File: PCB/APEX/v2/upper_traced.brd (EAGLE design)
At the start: 160 x 100 mm, 9 parts

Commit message: dimension boards
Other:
- board size 160 x 100 mm -> 72.4 x 23.8 mm
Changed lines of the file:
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@@
 <board>
 <plain>
-<wire x1="0" y1="0" x2="160" y2="0" width="0" layer="20"/>
-<wire x1="160" y1="0" x2="160" y2="100" width="0" layer="20"/>
-<wire x1="160" y1="100" x2="0" y2="100" width="0" layer="20"/>
-<wire x1="0" y1="100" x2="0" y2="0" width="0" layer="20"/>
-<dimension x1="7.62" y1="38.1" x2="80.01" y2="38.1" x3="43.815" y3="29.21" textsize="1.778" layer="1"/>
+<wire x1="7.62" y1="36.83" x2="79.99" y2="36.83" width="0" layer="20"/>
+<wire x1="79.99" y1="36.83" x2="79.99" y2="60.63" width="0" layer="20"/>
+<wire x1="79.99" y1="60.63" x2="7.62" y2="60.63" width="0" layer="20"/>
+<wire x1="7.62" y1="60.63" x2="7.62" y2="36.83" width="0" layer="20"/>
+<dimension x1="7.62" y1="36.83" x2="79.99" y2="36.83" x3="43.805" y3="33.02" textsize="1.778" layer="1"/>
+<dimension x1="79.99" y1="36.83" x2="79.99" y2="60.63" x3="83.82" y3="48.73" textsize="1.778" layer="1"/>
 </plain>
 <attributes>

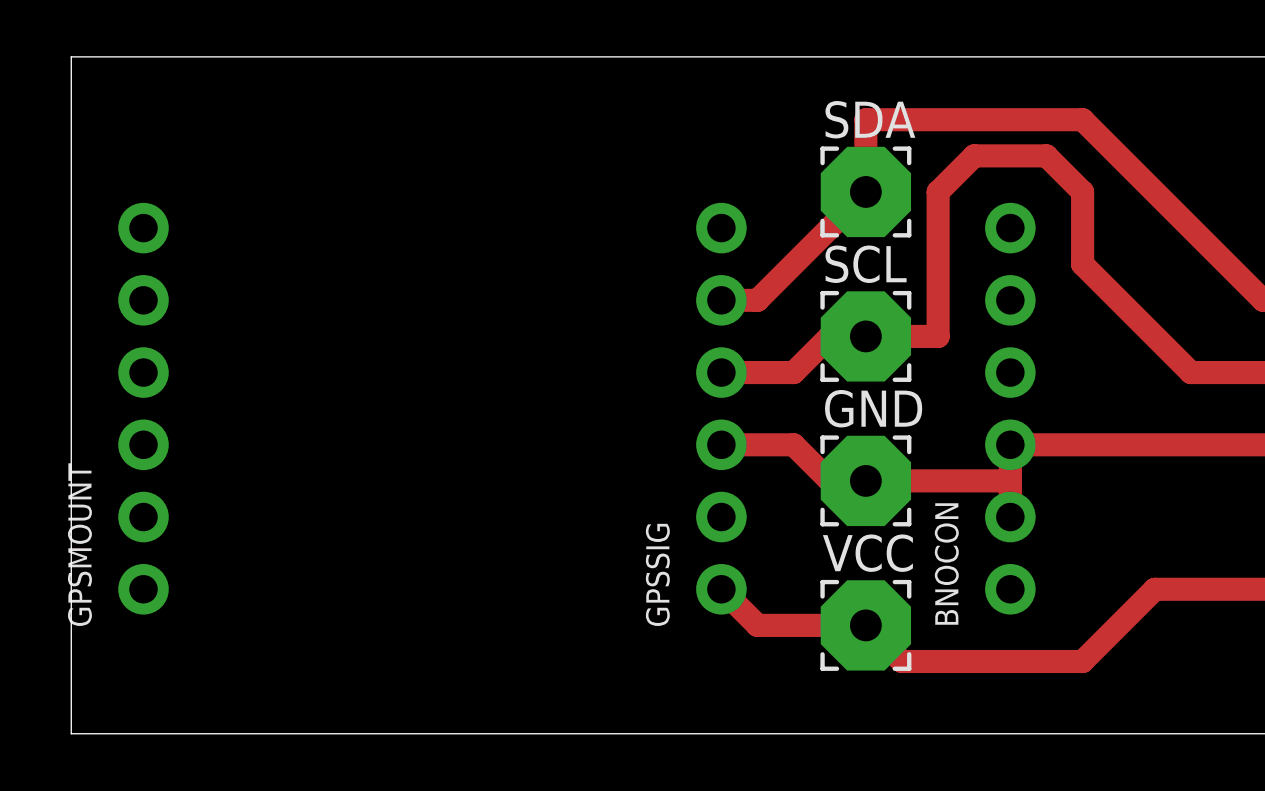
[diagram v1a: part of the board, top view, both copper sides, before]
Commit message: realign sim
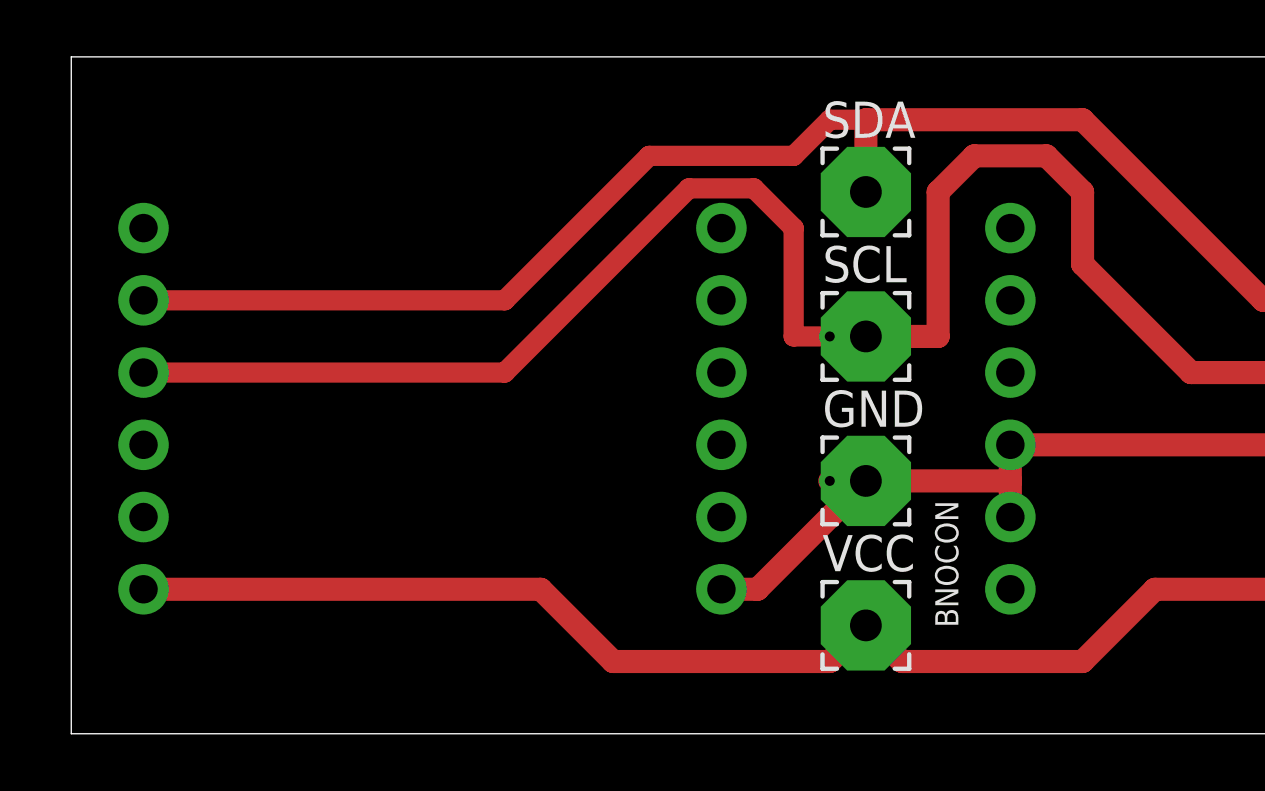
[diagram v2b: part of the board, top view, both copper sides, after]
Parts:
- moved GPSMOUNT 20.3 mm to (30.5, 48.3), flipped to the bottom
- moved GPSSIG 20.3 mm to (10.2, 48.3), flipped to the bottom
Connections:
- net GND: now also GPSMOUNT.1
- net VCC: now also GPSMOUNT.3
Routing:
- net SCL: track 58.3 -> 86.4 mm, vias 0 -> 1
- net VCC: track 49.6 -> 71.0 mm
- net SDA: track 54.3 -> 75.6 mm
- net GND: track 50.6 -> 52.9 mm, vias 0 -> 1
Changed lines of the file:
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@@
 <layer number="16" name="Bottom" color="1" fill="1" visible="yes" active="yes"/>
 <layer number="17" name="Pads" color="2" fill="1" visible="yes" active="yes"/>
-<layer number="18" name="Vias" color="2" fill="1" visible="yes" active="yes"/>
-<layer number="19" name="Unrouted" color="6" fill="1" visible="yes" active="yes"/>
-<layer number="20" name="Dimension" color="24" fill="1" visible="yes" active="yes"/>
-<layer number="21" name="tPlace" color="7" fill="1" visible="yes" active="yes"/>
+<layer number="18" name="Vias" color="2" fill="1" visible="no" active="yes"/>
+<layer number="19" name="Unrouted" color="6" fill="1" visible="no" active="yes"/>
+<layer number="20" name="Dimension" color="24" fill="1" visible="no" active="yes"/>
+<layer number="21" name="tPlace" color="7" fill="1" visible="no" active="yes"/>
 <layer number="22" name="bPlace" color="7" fill="1" visible="yes" active="yes"/>
-<layer number="23" name="tOrigins" color="15" fill="1" visible="yes" active="yes"/>
-<layer number="24" name="bOrigins" color="15" fill="1" visible="yes" active="yes"/>
-<layer number="25" name="tNames" color="7" fill="1" visible="yes" active="yes"/>
-<layer number="26" name="bNames" color="7" fill="1" visible="yes" active="yes"/>
-<layer number="27" name="tValues" color="7" fill="1" visible="yes" active="yes"/>
-<layer number="28" name="bValues" color="7" fill="1" visible="yes" active="yes"/>
+<layer number="23" name="tOrigins" color="15" fill="1" visible="no" active="yes"/>
+<layer number="24" name="bOrigins" color="15" fill="1" visible="no" active="yes"/>
+<layer number="25" name="tNames" color="7" fill="1" visible="no" active="yes"/>
+<layer number="26" name="bNames" color="7" fill="1" visible="no" active="yes"/>
+<layer number="27" name="tValues" color="7" fill="1" visible="no" active="yes"/>
+<layer number="28" name="bValues" color="7" fill="1" visible="no" active="yes"/>
 <layer number="29" name="tStop" color="7" fill="3" visible="no" active="yes"/>
 <layer number="30" name="bStop" color="7" fill="6" visible="no" active="yes"/>
@@
 <layer number="49" name="Reference" color="7" fill="1" visible="yes" active="yes"/>
 <layer number="50" name="dxf" color="7" fill="1" visible="no" active="no"/>
-<layer number="51" name="tDocu" color="7" fill="1" visible="yes" active="yes"/>
-<layer number="52" name="bDocu" color="7" fill="1" visible="yes" active="yes"/>
+<layer number="51" name="tDocu" color="7" fill="1" visible="no" active="yes"/>
+<layer number="52" name="bDocu" color="7" fill="1" visible="no" active="yes"/>
 <layer number="53" name="tGND_GNDA" color="7" fill="9" visible="no" active="no"/>
 <layer number="54" name="bGND_GNDA" color="1" fill="9" visible="no" active="no"/>
@@
 </layers>
 <board>
+<fusionsync huburn="a.YnVzaW5lc3M6bXlpYzM4OA" projecturn="a.YnVzaW5lc3M6bXlpYzM4OCMyMDIwMTEyMTM1NTQyNTgyNg" f3durn="urn:adsk.wipprod:dm.lineage:Sro-rczPQ5WDD7mKh9TVNQ" pcbguid="" lastpulledtime="" lastsyncedchangeguid="" latestrevisionid="8a8f237b-fe8f-4934-b37e-711cd0af9fbb" lastsyncedrevisionid="8a8f237b-fe8f-4934-b37e-711cd0af9fbb" lastboardhashguid="14b4f4f1-fdd0-a5f1-0295-8ed9d9b95309" lastpushedtime="2021-07-01T21:12:17Z" linktopcb3d="true"/>
 <plain>
 <wire x1="7.62" y1="36.83" x2="79.99" y2="36.83" width="0" layer="20"/>
@@
 <wire x1="79.99" y1="60.63" x2="7.62" y2="60.63" width="0" layer="20"/>
 <wire x1="7.62" y1="60.63" x2="7.62" y2="36.83" width="0" layer="20"/>
-<dimension x1="7.62" y1="36.83" x2="79.99" y2="36.83" x3="43.805" y3="33.02" textsize="1.778" layer="1"/>
-<dimension x1="79.99" y1="36.83" x2="79.99" y2="60.63" x3="83.82" y3="48.73" textsize="1.778" layer="1"/>
 </plain>
 <attributes>
@@
 <attribute name="VALUE" x="80.645" y="39.37" size="0.4064" layer="27" ratio="10" rot="R90"/>
 </element>
-<element name="GPSSIG" library="microbuilder" package="1X06_ROUND_70" value="" x="30.48" y="48.26" smashed="yes" rot="R90">
-<attribute name="NAME" x="28.6512" y="40.5638" size="0.8128" layer="25" ratio="18" rot="R90"/>
-<attribute name="VALUE" x="32.385" y="40.64" size="0.4064" layer="27" ratio="10" rot="R90"/>
-</element>
-<element name="GPSMOUNT" library="microbuilder" package="1X06_ROUND_70" value="" x="10.16" y="48.26" smashed="yes" rot="R90">
-<attribute name="NAME" x="8.3312" y="40.5638" size="0.8128" layer="25" ratio="18" rot="R90"/>
-<attribute name="VALUE" x="13.335" y="40.64" size="0.4064" layer="27" ratio="10" rot="R90"/>
+<element name="GPSSIG" library="microbuilder" package="1X06_ROUND_70" value="" x="10.16" y="48.26" smashed="yes" rot="MR90">
+<attribute name="NAME" x="11.9888" y="40.5638" size="0.8128" layer="26" ratio="18" rot="MR90"/>
+<attribute name="VALUE" x="8.255" y="40.64" size="0.4064" layer="28" ratio="10" rot="MR90"/>
+</element>
+<element name="GPSMOUNT" library="microbuilder" package="1X06_ROUND_70" value="" x="30.48" y="48.26" smashed="yes" rot="MR90">
+<attribute name="NAME" x="32.3088" y="40.5638" size="0.8128" layer="26" ratio="18" rot="MR90"/>
+<attribute name="VALUE" x="27.305" y="40.64" size="0.4064" layer="28" ratio="10" rot="MR90"/>
 </element>
 <element name="SCL" library="wirepad" library_urn="urn:adsk.eagle:library:412" package="3,17/1,1" package3d_urn="urn:adsk.eagle:package:30832/1" value="" x="35.56" y="50.8" smashed="yes">
@@
 <wire x1="58.42" y1="46.99" x2="69.85" y2="46.99" width="0.8128" layer="1"/>
 <wire x1="35.56" y1="45.72" x2="34.29" y2="45.72" width="0.8128" layer="1"/>
-<wire x1="34.29" y1="45.72" x2="33.02" y2="46.99" width="0.8128" layer="1"/>
-<wire x1="33.02" y1="46.99" x2="30.48" y2="46.99" width="0.8128" layer="1"/>
 <wire x1="35.56" y1="45.72" x2="40.64" y2="45.72" width="0.8128" layer="1"/>
+<via x="34.29" y="45.72" extent="1-16" drill="0.35"/>
+<contactref element="GPSMOUNT" pad="1"/>
+<wire x1="35.56" y1="45.72" x2="31.75" y2="41.91" width="0.8128" layer="1"/>
+<wire x1="31.75" y1="41.91" x2="30.48" y2="41.91" width="0.8128" layer="1"/>
+<wire x1="10.16" y1="46.99" x2="30.48" y2="41.91" width="0" layer="19" extent="1-1"/>
 </signal>
 <signal name="VCC" class="2">
@@
 <wire x1="36.83" y1="39.37" x2="43.18" y2="39.37" width="0.8128" layer="1"/>
 <wire x1="43.18" y1="39.37" x2="45.72" y2="41.91" width="0.8128" layer="1"/>
-<wire x1="35.56" y1="40.64" x2="31.75" y2="40.64" width="0.8128" layer="1"/>
-<wire x1="31.75" y1="40.64" x2="30.48" y2="41.91" width="0.8128" layer="1"/>
+<contactref element="GPSMOUNT" pad="3"/>
+<wire x1="35.56" y1="40.64" x2="34.29" y2="39.37" width="0.8128" layer="1"/>
+<wire x1="24.13" y1="41.91" x2="10.16" y2="41.91" width="0.8128" layer="1"/>
+<wire x1="34.29" y1="39.37" x2="26.67" y2="39.37" width="0.8128" layer="1"/>
+<wire x1="26.67" y1="39.37" x2="24.13" y2="41.91" width="0.8128" layer="1"/>
 <wire x1="35.56" y1="40.64" x2="40.64" y2="49.53" width="0" layer="19" extent="1-1"/>
+<wire x1="30.48" y1="46.99" x2="35.56" y2="40.64" width="0" layer="19" extent="1-1"/>
 </signal>
 <signal name="SDA">
@@
 <wire x1="35.56" y1="55.88" x2="35.56" y2="58.42" width="0.8128" layer="1"/>
 <wire x1="49.53" y1="52.07" x2="58.42" y2="52.07" width="0.8128" layer="1"/>
-<wire x1="35.56" y1="58.42" x2="43.18" y2="58.42" width="0.8128" layer="1"/>
+<wire x1="43.18" y1="58.42" x2="35.56" y2="58.42" width="0.8128" layer="1"/>
 <wire x1="43.18" y1="58.42" x2="49.53" y2="52.07" width="0.8128" layer="1"/>
-<wire x1="30.48" y1="52.07" x2="31.75" y2="52.07" width="0.8128" layer="1"/>
-<wire x1="31.75" y1="52.07" x2="35.56" y2="55.88" width="0.8128" layer="1"/>
+<wire x1="35.56" y1="58.42" x2="34.29" y2="58.42" width="0.7112" layer="1"/>
+<wire x1="34.29" y1="58.42" x2="33.02" y2="57.15" width="0.7112" layer="1"/>
+<wire x1="27.94" y1="57.15" x2="22.86" y2="52.07" width="0.7112" layer="1"/>
+<wire x1="22.86" y1="52.07" x2="10.16" y2="52.07" width="0.7112" layer="1"/>
+<wire x1="33.02" y1="57.15" x2="27.94" y2="57.15" width="0.7112" layer="1"/>
 </signal>
 <signal name="SCL">
@@
 <wire x1="43.18" y1="53.34" x2="43.18" y2="55.88" width="0.8128" layer="1"/>
 <wire x1="35.56" y1="50.8" x2="34.29" y2="50.8" width="0.8128" layer="1"/>
-<wire x1="34.29" y1="50.8" x2="33.02" y2="49.53" width="0.8128" layer="1"/>
-<wire x1="33.02" y1="49.53" x2="30.48" y2="49.53" width="0.8128" layer="1"/>
+<via x="34.29" y="50.8" extent="1-16" drill="0.35"/>
+<wire x1="35.56" y1="50.8" x2="33.02" y2="50.8" width="0.7112" layer="1"/>
+<wire x1="33.02" y1="50.8" x2="33.02" y2="54.61" width="0.7112" layer="1"/>
+<wire x1="33.02" y1="54.61" x2="31.623" y2="56.007" width="0.7112" layer="1"/>
+<wire x1="31.623" y1="56.007" x2="29.337" y2="56.007" width="0.7112" layer="1"/>
+<wire x1="29.337" y1="56.007" x2="22.86" y2="49.53" width="0.7112" layer="1"/>
+<wire x1="22.86" y1="49.53" x2="10.16" y2="49.53" width="0.7112" layer="1"/>
 </signal>
 <signal name="+3V3">
@@
 <contactref element="BARO" pad="2"/>
 <wire x1="58.42" y1="44.45" x2="77.47" y2="43.18" width="0" layer="19" extent="1-1"/>
-<wire x1="30.48" y1="44.45" x2="58.42" y2="44.45" width="0" layer="19" extent="1-1"/>
+<wire x1="10.16" y1="44.45" x2="58.42" y2="44.45" width="0" layer="19" extent="1-1"/>
 </signal>
 </signals>
@@
 </note>
 <note version="8.3" severity="warning">
+Since Version 8.3, EAGLE supports Fusion synchronisation.
+This feature will not be available in this version and saving
+the document will break the link to the Fusion PCB feature.
+</note>
+<note version="8.3" severity="warning">
